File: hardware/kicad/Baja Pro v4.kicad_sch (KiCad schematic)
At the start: 23 parts, among them J1 Thermistor, P1 Remote, P2 Power, P4 Flash, U1 FM24CL04B-GTR_C365762, U2 DC-DC stepdown, U3 AMS1117-3.3, U4 ESP32-WROOM-32

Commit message: Implement on board DCDC converter Run on 3.3V Replace thermistor with SMD one Change cable connectors to JST Rearrange tracks to help WiFi antenna clearance
Signed-off-by: Ilias Daradimos <judgedrid@gmail.com>
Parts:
- removed U2: DC-DC stepdown, Baja Pro v4:DC-DC STEPDOWN, symbol BajaPro:DC-DC Stepdown
- removed U3: AMS1117-3.3, Package_TO_SOT_SMD:SOT-223-3_TabPin2, symbol Regulator_Linear:AMS1117-3.3
- added C7: 100nF, Capacitor_SMD:C_0805_2012Metric_Pad1.18x1.45mm_HandSolder, symbol Device:C
- added C8: 47pF, Capacitor_SMD:C_0603_1608Metric_Pad1.08x0.95mm_HandSolder, symbol Device:C
- added C9: 47uF, Capacitor_SMD:C_1210_3225Metric_Pad1.33x2.70mm_HandSolder, symbol Device:C
- added L1: 10uH, Inductor_SMD:L_Bourns_SRP5030T, symbol Device:L
- added R7: 100k, Resistor_SMD:R_0603_1608Metric_Pad0.98x0.95mm_HandSolder, symbol Device:R
- added R8: 22k, Resistor_SMD:R_0603_1608Metric_Pad0.98x0.95mm_HandSolder, symbol Device:R
- added U2: TPS54302, Package_TO_SOT_SMD:SOT-23-6, symbol Regulator_Switching:TPS54302
- C1, C2, C3, C4, C5: footprint Baja Pro v4:1206 -> Capacitor_SMD:C_1206_3216Metric_Pad1.33x1.80mm_HandSolder
- C6: value 22uF -> 10uF; footprint Baja Pro v4:1206 -> Capacitor_SMD:C_1210_3225Metric_Pad1.33x2.70mm_HandSolder; Manufacturer FH -> (none); Manufacturer Part 1206B226K160NT -> (none); PartNumber (none) -> CL32A106KBJNNNE; Supplier LCSC -> (none); Supplier Part C31847 -> (none)
- J1: value Thermistor -> NTC 10K±1% 3950; footprint Connector_PinHeader_2.54mm:PinHeader_1x02_P2.54mm_Vertical -> Resistor_SMD:R_0805_2012Metric_Pad1.20x1.40mm_HandSolder; symbol Connector_Generic:Conn_01x02 -> Device:Thermistor_NTC
- P1: footprint Connector_PinHeader_2.54mm:PinHeader_1x04_P2.54mm_Vertical -> Connector_JST:JST_XH_S4B-XH-A_1x04_P2.50mm_Horizontal
- P2: footprint Connector_PinHeader_2.54mm:PinHeader_1x02_P2.54mm_Vertical -> Connector_JST:JST_XH_S2B-XH-A_1x02_P2.50mm_Horizontal
- R1, R2, R3, R4, R5, R6: footprint Baja Pro v4:1206 -> Resistor_SMD:R_1206_3216Metric_Pad1.30x1.75mm_HandSolder
- U1: footprint Baja Pro v4:SOIC-8_150MIL -> Package_SO:SOIC-8_3.9x4.9mm_P1.27mm
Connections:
- net 5V is gone; now on net 3V3: GPS1.4 (VCC), J1.2
- net 3V3: now also C8.1, C9.1, L1.2, R7.1; no longer C6.2
- net GND: now also C6.2, C9.2, R8.2, U2.1 (GND); no longer C6.1
- net VIN: now reaches D1.1 (K)
- net VIN: now also C6.1, U2.3 (VIN)
- new net: C7.2, L1.1, U2.2 (SW)
- new net: C8.2, R7.2, R8.1, U2.4 (FB)
- new net: C7.1, U2.6 (BOOT)
- no-connect marks 15 -> 16
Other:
- moved on the sheet: D1

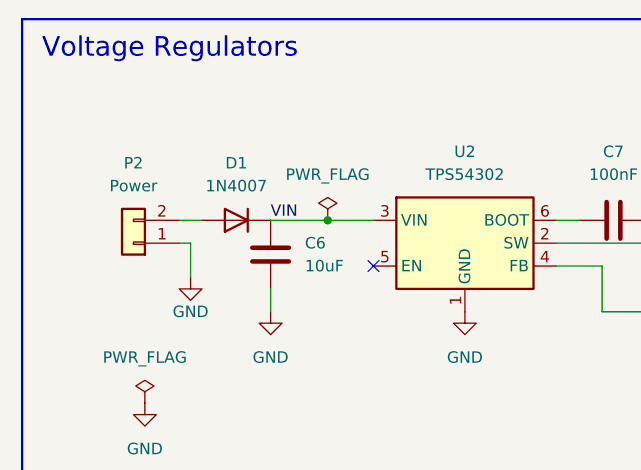
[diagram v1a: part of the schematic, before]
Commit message: Add part numbers Generate BOM Generate HTML assembly
Signed-off-by: Ilias Daradimos <judgedrid@gmail.com>
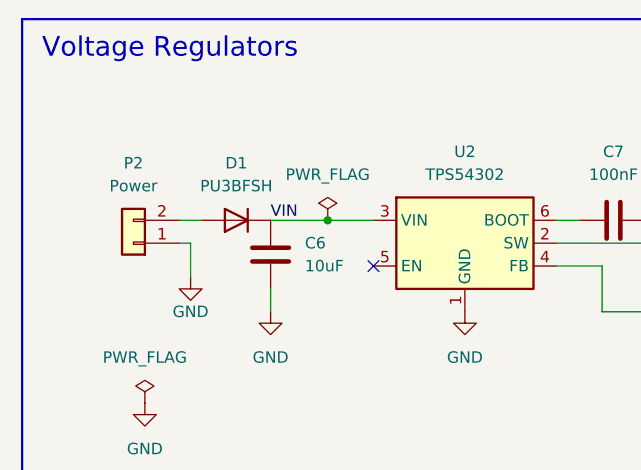
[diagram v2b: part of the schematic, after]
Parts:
- C1, C2: Manufacturer Part (none) -> C1206C225K5RECAUTO7210
- C3: Manufacturer Part (none) -> C1206C334K1RECAUTO7210
- C4: Manufacturer Part (none) -> C1206C104K5RACAUTO7210
- C5: Manufacturer Part (none) -> CL32A106KBJNNNE
- C6: footprint Capacitor_SMD:C_1210_3225Metric_Pad1.33x2.70mm_HandSolder -> Capacitor_SMD:C_1206_3216Metric_Pad1.33x1.80mm_HandSolder; Manufacturer Part (none) -> CL32A106KBJNNNE; PartNumber CL32A106KBJNNNE -> (none)
- C7: Manufacturer Part (none) -> C0805C104M5RACTU; PartNumber C0805C104M5RACTU -> (none)
- C8: Manufacturer Part (none) -> C1206C470K5GACAUTO
- C9: Manufacturer Part (none) -> GRM32ER61C476KE15L; PartNumber GRM32ER61C476KE15L -> (none)
- D1: value 1N4007 -> PU3BFSH; footprint Diode_SMD:D_SOD-123F -> Diode_SMD:D_SOD-128; Manufacturer Part (none) -> PU3BFSH
- J1: Manufacturer Part (none) -> ABNTC-0805-103J-3950F-T
- L1: Manufacturer Part (none) -> SRP5030T-5R6M; PartNumber SRP5030T-5R6M -> (none)
- P1: Manufacturer Part (none) -> S4B-XH-A
- P2: Manufacturer Part (none) -> S2B-XH-A
- P4: Manufacturer Part (none) -> Pin Header 2.54
- R1: Manufacturer Part (none) -> MCA1206MD1005BP500
- R2: Manufacturer Part (none) -> RN73R2BTTD1001F50
- R3, R4: Manufacturer Part (none) -> RG3216P-2401-D-T5
- R5, R6: Manufacturer Part (none) -> RG3216P-1002-D-T5
- R7: Manufacturer Part (none) -> CRCW0604100KFKED; PartNumber CRCW0604100KFKED -> (none)
- R8: Manufacturer Part (none) -> RC0603FR-0722KL; PartNumber RC0603FR-0722KL -> (none)
- U2: Manufacturer Part (none) -> TPS54302DDCR; PartNumber TPS54302DDCR -> (none)
- U4: Manufacturer Part (none) -> ESP32-WROOM-32
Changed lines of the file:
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@@
 			)
 		)
-		(property "Value" "1N4007"
+		(property "Value" "PU3BFSH"
 			(at 43.18 43.18 0)
 			(effects
@@
 			)
 		)
-		(property "Footprint" "Diode_SMD:D_SOD-123F"
+		(property "Footprint" "Diode_SMD:D_SOD-128"
 			(at 43.18 46.99 0)
 			(effects
@@
 			)
 		)
+		(property "Manufacturer Part" "PU3BFSH"
+			(at 43.18 46.99 0)
+			(effects
+				(font
+					(size 1.27 1.27)
+				)
+				(hide yes)
+			)
+		)
 		(pin "2"
 		)
@@
 			)
 		)
+		(property "Manufacturer Part" "C1206C104K5RACAUTO7210"
+			(at 78.74 222.25 0)
+			(effects
+				(font
+					(size 1.27 1.27)
+				)
+				(hide yes)
+			)
+		)
 		(pin "1"
 		)
@@
 			)
 		)
-		(property "PartNumber" "  SRP5030T-5R6M"
+		(property "Manufacturer Part" "  SRP5030T-5R6M"
 			(at 95.25 49.53 90)
 			(effects
@@
 			)
 		)
+		(property "Manufacturer Part" "MCA1206MD1005BP500"
+			(at 73.66 254 90)
+			(effects
+				(font
+					(size 1.27 1.27)
+				)
+				(hide yes)
+			)
+		)
 		(pin "1"
 		)
@@
 			)
 		)
+		(property "Manufacturer Part" "RG3216P-2401-D-T5"
+			(at 248.92 54.61 0)
+			(effects
+				(font
+					(size 1.27 1.27)
+				)
+				(hide yes)
+			)
+		)
 		(pin "1"
 		)
@@
 			)
 		)
+		(property "Manufacturer Part" "RG3216P-2401-D-T5"
+			(at 224.79 48.26 0)
+			(effects
+				(font
+					(size 1.27 1.27)
+				)
+				(hide yes)
+			)
+		)
 		(pin "2"
 		)
@@
 			)
 		)
+		(property "Manufacturer Part" "CL32A106KBJNNNE"
+			(at 86.36 222.25 0)
+			(effects
+				(font
+					(size 1.27 1.27)
+				)
+				(hide yes)
+			)
+		)
 		(pin "1"
 		)
@@
 			)
 		)
+		(property "Manufacturer Part" "ABNTC-0805-103J-3950F-T"
+			(at 382.27 245.11 0)
+			(effects
+				(font
+					(size 1.27 1.27)
+				)
+				(hide yes)
+			)
+		)
 		(pin "2"
 		)
@@
 			)
 		)
+		(property "Manufacturer Part" "RN73R2BTTD1001F50"
+			(at 364.49 240.03 90)
+			(effects
+				(font
+					(size 1.27 1.27)
+				)
+				(hide yes)
+			)
+		)
 		(pin "2"
 		)
@@
 			)
 		)
-		(property "PartNumber" "RC0603FR-0722KL"
+		(property "Manufacturer Part" "RC0603FR-0722KL"
 			(at 111.76 60.96 0)
 			(effects
@@
 			)
 		)
+		(property "Manufacturer Part" "C1206C225K5RECAUTO7210"
+			(at 96.52 233.68 0)
+			(effects
+				(font
+					(size 1.27 1.27)
+				)
+				(hide yes)
+			)
+		)
 		(pin "2"
 		)
@@
 			)
 		)
-		(property "PartNumber" "CRCW0604100KFKED"
+		(property "Manufacturer Part" "CRCW0604100KFKED"
 			(at 111.76 53.34 0)
 			(effects
@@
 			)
 		)
-		(property "PartNumber" "C0805C104M5RACTU"
+		(property "Manufacturer Part" "C0805C104M5RACTU"
 			(at 85.09 46.99 90)
 			(effects
@@
 			)
 		)
+		(property "Manufacturer Part" "C1206C470K5GACAUTO"
+			(at 101.6 53.34 0)
+			(effects
+				(font
+					(size 1.27 1.27)
+				)
+				(hide yes)
+			)
+		)
 		(pin "1"
 		)
@@
 			)
 		)
+		(property "Manufacturer Part" "Pin Header 2.54"
+			(at 368.3 125.73 0)
+			(effects
+				(font
+					(size 1.27 1.27)
+				)
+				(hide yes)
+			)
+		)
 		(pin "5"
 		)
@@
 			)
 		)
+		(property "Manufacturer Part" "S2B-XH-A"
+			(at 31.75 49.53 0)
+			(effects
+				(font
+					(size 1.27 1.27)
+				)
+				(hide yes)
+			)
+		)
 		(pin "1"
 		)
@@
 			)
 		)
-		(property "Footprint" "Capacitor_SMD:C_1210_3225Metric_Pad1.33x2.70mm_HandSolder"
+		(property "Footprint" "Capacitor_SMD:C_1206_3216Metric_Pad1.33x1.80mm_HandSolder"
 			(at 47.9552 54.61 0)
 			(effects
@@
 			)
 		)
-		(property "PartNumber" "CL32A106KBJNNNE"
+		(property "Manufacturer Part" "CL32A106KBJNNNE"
 			(at 46.99 50.8 0)
 			(effects
@@
 			)
 		)
+		(property "Manufacturer Part" "C1206C334K1RECAUTO7210"
+			(at 73.66 243.84 90)
+			(effects
+				(font
+					(size 1.27 1.27)
+				)
+				(hide yes)
+			)
+		)
 		(pin "2"
 		)
@@
 			)
 		)
+		(property "Manufacturer Part" "ESP32-WROOM-32"
+			(at 210.82 203.2 0)
+			(effects
+				(font
+					(size 1.27 1.27)
+				)
+				(hide yes)
+			)
+		)
 		(pin "8"
 		)
@@
 			)
 		)
+		(property "Manufacturer Part" "S4B-XH-A"
+			(at 374.65 177.8 0)
+			(effects
+				(font
+					(size 1.27 1.27)
+				)
+				(hide yes)
+			)
+		)
 		(pin "2"
 		)
@@
 			)
 		)
+		(property "Manufacturer Part" "C1206C225K5RECAUTO7210"
+			(at 90.17 240.03 0)
+			(effects
+				(font
+					(size 1.27 1.27)
+				)
+				(hide yes)
+			)
+		)
 		(pin "2"
 		)
@@
 			)
 		)
-		(property "PartNumber" "TPS54302DDCR"
+		(property "Manufacturer Part" "TPS54302DDCR"
 			(at 68.58 49.53 0)
 			(effects
@@
 			)
 		)
+		(property "Manufacturer Part" "RG3216P-1002-D-T5"
+			(at 231.14 242.57 0)
+			(effects
+				(font
+					(size 1.27 1.27)
+				)
+				(hide yes)
+			)
+		)
 		(pin "1"
 		)
@@
 			)
 		)
+		(property "Manufacturer Part" "RG3216P-1002-D-T5"
+			(at 190.5 163.83 0)
+			(effects
+				(font
+					(size 1.27 1.27)
+				)
+				(hide yes)
+			)
+		)
 		(pin "1"
 		)
@@
 			)
 		)
-		(property "PartNumber" "GRM32ER61C476KE15L"
+		(property "Manufacturer Part" "GRM32ER61C476KE15L"
 			(at 123.19 53.34 0)
 			(effects
